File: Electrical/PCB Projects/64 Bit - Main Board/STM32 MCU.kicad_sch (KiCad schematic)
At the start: 21 parts, among them U1 STM32F446RETx, Y1 Crystal_GND24, Y2 32.768kHz-12.6pF

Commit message: finalized schematic, made ESP32 footprint, started PCB update
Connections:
- no-connect marks 8 -> 7
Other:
- note added: "ADC3 input 11"

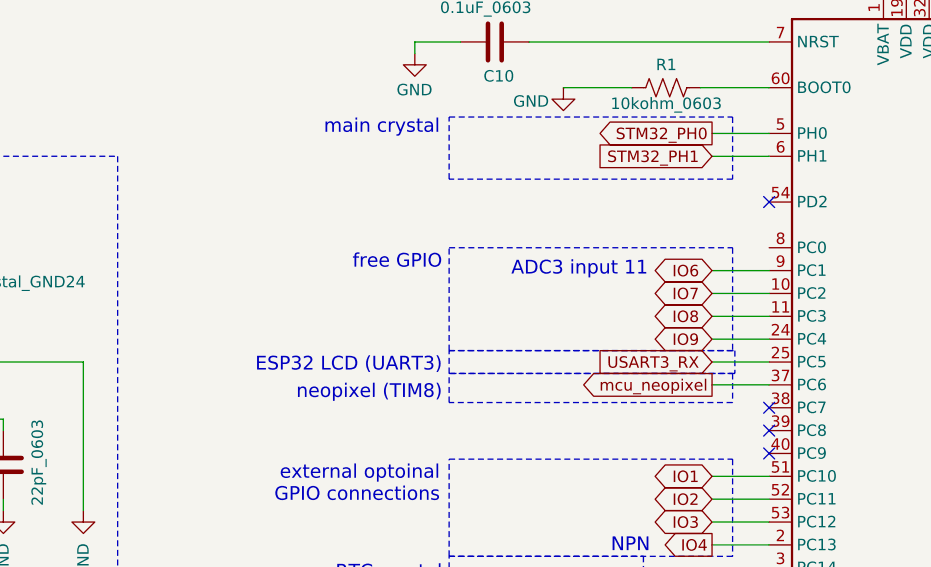
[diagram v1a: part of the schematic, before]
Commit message: finished routing - added photoresistor to analog pin. Updated STM32Cube setup. Final stages of hardware design
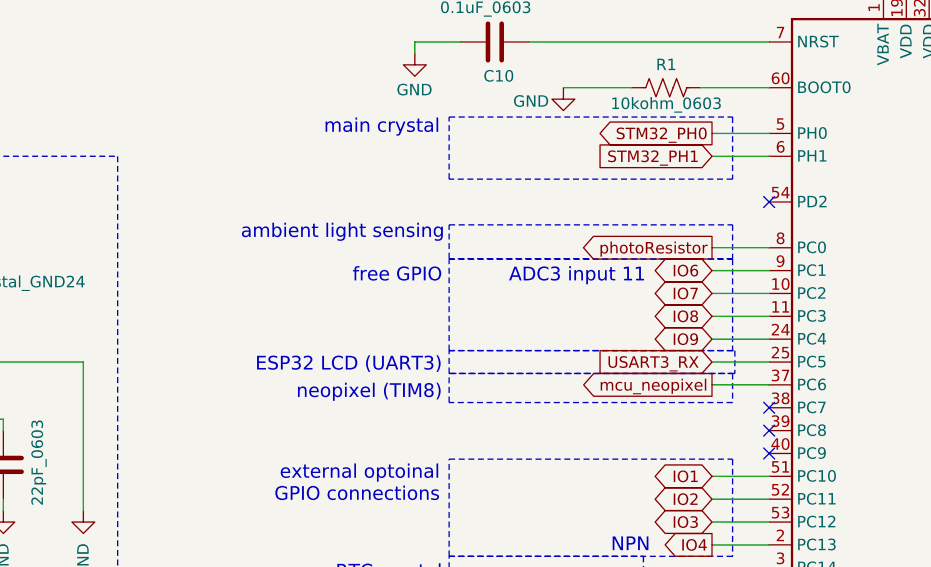
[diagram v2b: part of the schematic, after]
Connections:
- net photoResistor: now reaches U1.8 (PC0)
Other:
- note added: "ambient light sensing"
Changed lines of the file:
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@@
+	)
+	(rectangle
+		(start 107.9499 71.12)
+		(end 139.4459 74.8783)
+		(stroke
+			(width 0)
+			(type dash)
+			(color 72 73 255 1)
+		)
+		(fill
+			(type none)
+		)
 	)
 	(rectangle
@@
 	)
 	(rectangle
-		(start 107.95 73.66)
+		(start 107.95 74.93)
 		(end 139.446 85.09)
 		(stroke
@@
 	(text "free GPIO"
 		(exclude_from_sim no)
-		(at 107.188 76.2 0)
+		(at 107.188 77.724 0)
 		(effects
 			(font
@@
 	(text "ADC3 input 11"
 		(exclude_from_sim no)
-		(at 130.048 76.962 0)
+		(at 129.794 77.724 0)
 		(effects
 			(font
@@
 			)
 			(justify left bottom)
+		)
+	)
+	(text "ambient light sensing"
+		(exclude_from_sim no)
+		(at 107.442 72.898 0)
+		(effects
+			(font
+				(size 1.524 1.524)
+				(thickness 0.1905)
+			)
+			(justify right bottom)
 		)
 	)
@@
 		(pts
 			(xy 179.07 114.3) (xy 183.134 114.3)
+		)
+		(stroke
+			(width 0)
+			(type default)
+		)
+	)
+	(wire
+		(pts
+			(xy 137.16 73.66) (xy 143.51 73.66)
 		)
 		(stroke
@@
 				(hide yes)
 			)
+		)
+	)
+	(global_label "photoResistor"
+		(shape output)
+		(at 137.16 73.66 180)
+		(fields_autoplaced yes)
+		(effects
+			(font
+				(size 1.27 1.27)
+			)
+			(justify right)
+		)
+		(property "Intersheetrefs" "${INTERSHEET_REFS}"
+			(at 121.1726 73.66 0)
+			(effects
+				(font
+					(size 1.27 1.27)
+				)
+				(justify right)
+				(hide yes)
+			)
